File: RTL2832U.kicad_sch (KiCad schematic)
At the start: 35 parts, among them U3 RTL2832U, U4 M24C02-WMN

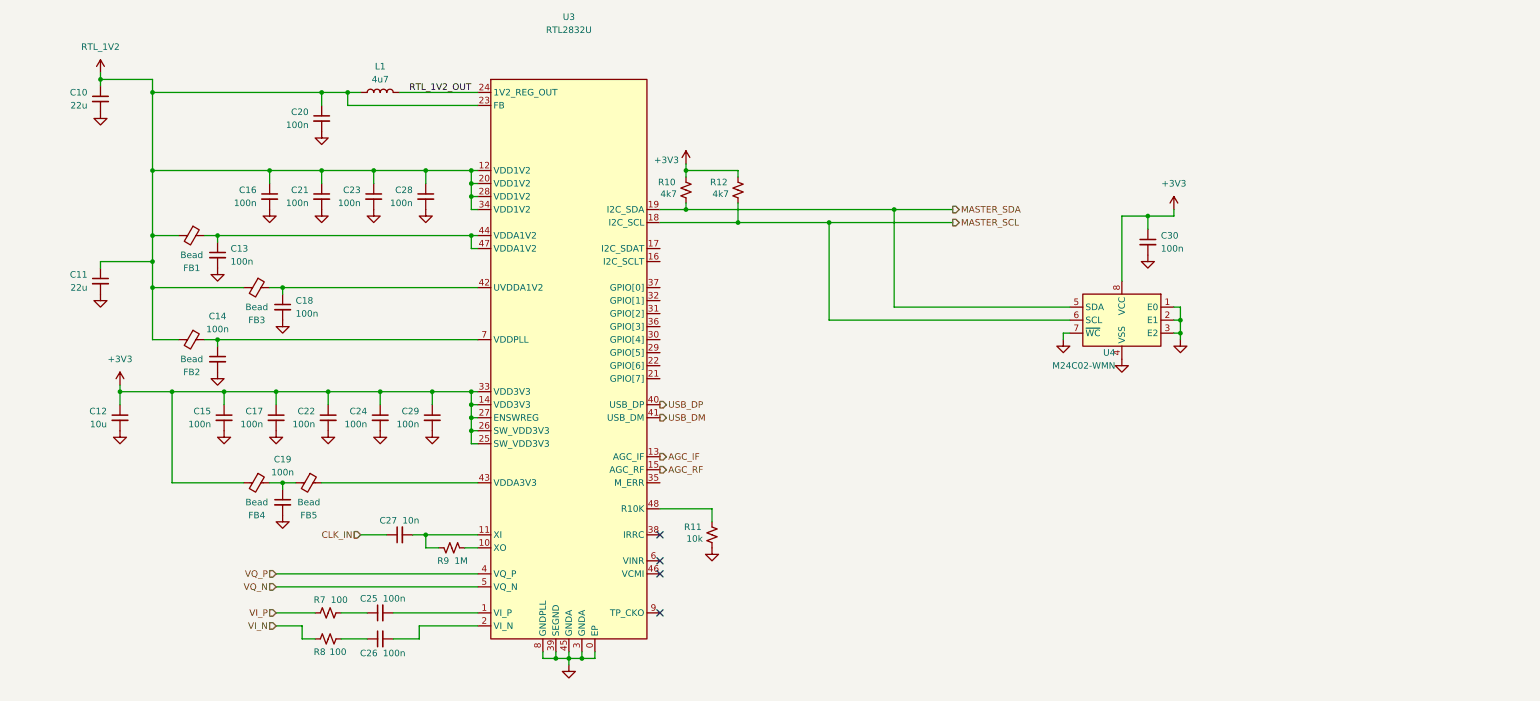
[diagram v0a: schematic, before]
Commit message: Schematic progress
I keep forgetting that I'm just making a panadapter here and not a full blown SDR...oops
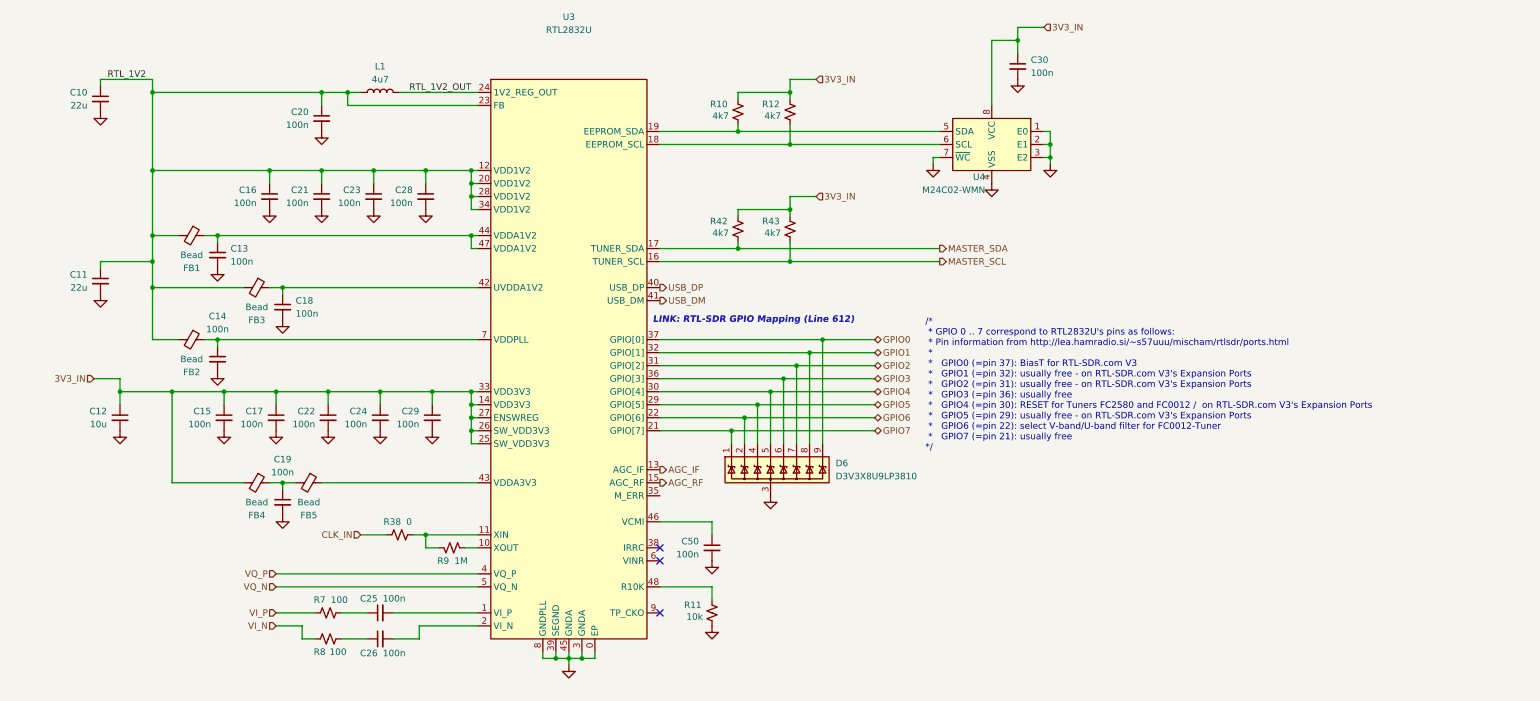
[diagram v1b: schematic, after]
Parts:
- removed C27: 10n, libraries:Worthington_C_0402, symbol Device:C_Small
- added C50: 100n, libraries:Worthington_C_0402, symbol Device:C_Small
- added D6: D3V3X8U9LP3810, Package_DFN_QFN:Diodes_UDFN3810-9_TYPE_B, symbol Power_Protection:D3V3X8U9LP3810
- added R38: 0, libraries:Worthington_R_0402, symbol Device:R_Small_US
- added R42, R43: 4k7, libraries:Worthington_R_0402, symbol Device:R_Small_US
- R10, R11, R12, R7, R8, R9: footprint (none) -> libraries:Worthington_R_0402
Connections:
- net CLK_IN: now also R38.1
- net GND: now also C50.2, D6.3 (GND)
- net MASTER_SCL: now also U3.16 (TUNER_SCL), R43.1; no longer R12.1, U3.18 (I2C_SCL), U4.6 (SCL)
- net MASTER_SDA: now also U3.17 (TUNER_SDA), R42.1; no longer R10.1, U3.19 (I2C_SDA), U4.5 (SDA)
- net at R9.1, U3.11 (XIN): now also R38.2
- net GPIO7: now reaches U3.21 (GPIO[7])
- net GPIO7: now also D6.1 (Line-1)
- net GPIO6: now reaches U3.22 (GPIO[6])
- net GPIO6: now also D6.2 (Line-3)
- net GPIO5: now reaches U3.29 (GPIO[5])
- net GPIO5: now also D6.4 (Line-6)
- net GPIO4: now reaches U3.30 (GPIO[4])
- net GPIO4: now also D6.5 (Line-8)
- net GPIO2: now reaches U3.31 (GPIO[2])
- net GPIO2: now also D6.7 (Line-5)
- net GPIO1: now reaches U3.32 (GPIO[1])
- net GPIO1: now also D6.8 (Line-4)
- net GPIO3: now reaches U3.36 (GPIO[3])
- net GPIO3: now also D6.6 (Line-7)
- net GPIO0: now reaches U3.37 (GPIO[0])
- net GPIO0: now also D6.9 (Line-2)
- net at U3.46 (VCMI): now also C50.1
- net +3V3 renamed 3V3_IN
- net 3V3_IN: now also R42.2, R43.2
- new net: R12.1, U3.18 (EEPROM_SCL), U4.6 (SCL)
- new net: R10.1, U3.19 (EEPROM_SDA), U4.5 (SDA)
- no-connect marks 4 -> 3
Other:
- note added: "/* * GPIO 0 .. 7 correspond to RTL2832U's pins as follows: * Pin information from http://lea.hamradio.si/~s57uuu/mischam/rtlsdr/ports.html * * GPIO0 (=pin 37): BiasT for RTL-SDR.com V3 * GPIO1 (=pin 32): usually free - on RTL-SDR.com V3's Expansion Ports * GPIO2 (=pin 31): usually free - on RTL-SDR.com V3's Expansion Ports * GPIO3 (=pin 36): usually free * GPIO4 (=pin 30): RESET for Tuners FC2580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"
- note added: "LINK: RTL-SDR GPIO Mapping (Line 612)"
- moved on the sheet: C30, R10, R11, R12, U4

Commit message: Schematic progress
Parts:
- added C90, C91: 100n, libraries:Worthington_C_0402, symbol Device:C_Small
- added R37, R68: 100, libraries:Worthington_R_0402, symbol Device:R_Small_US
- added R69, R70: 50, libraries:Worthington_R_0402, symbol Device:R_Small_US
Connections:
- net VI_N: now also R70.1
- net VI_P: now also R70.2
- net VQ_N: now also R68.2, R69.1; no longer U3.5 (VQ_N)
- net VQ_P: now also R37.1, R69.2; no longer U3.4 (VQ_P)
- new net: C90.1, R37.2
- new net: C90.2, U3.4 (VQ_P)
- new net: C91.2, U3.5 (VQ_N)
- new net: C91.1, R68.1
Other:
- note added: "90-Ohm Trace Impedance"
- moved on the sheet: C25, C26, R7, R8, U3

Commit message: Schematic progress
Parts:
- removed C10, C11: 22u, libraries:Worthington_C_0603, symbol Device:C_Small
- removed C12: 10u, libraries:Worthington_C_0603, symbol Device:C_Small
- removed C13, C14, C15, C16, C17, C18, C19, C20, C21, C22, C23, C24, C25, C26, C28, C29, C30, C50: 100n, libraries:Worthington_C_0402, symbol Device:C_Small
- removed R10, R12: 4k7, libraries:Worthington_R_0402, symbol Device:R_Small_US
- removed R38: 0, libraries:Worthington_R_0402, symbol Device:R_Small_US
- added C100, C101, C102, C103, C104, C105, C106, C107, C108, C109, C110, C111, C112, C113, C114, C115, C124, C98, C99: 100n, libraries:Worthington_C_0201, symbol Device:C_Small
- added C125, C126, C53: 10u, libraries:Worthington_C_0402, symbol Device:C_Small
- added R73, R74: 4k7, libraries:Worthington_R_0201, symbol Device:R_Small_US
- added R75, R76: 0, libraries:Worthington_R_0201, symbol Device:R_Small_US
- C90, C91: footprint libraries:Worthington_C_0402 -> libraries:Worthington_C_0201; DigiKey (none) -> 445-15903-1-ND; Manufacturer Part Number (none) -> C0603X6S1C104K030BC; Voltage (none) -> 16V
- FB1, FB2, FB3, FB4, FB5: footprint (none) -> libraries:Worthington_L_0402; now not fitted
- L1: value 4u7 -> 4u7,±20%; footprint Inductor_SMD:L_0805_2012Metric -> Inductor_SMD:L_1008_2520Metric; Current (none) -> 1.5A; DC Resistance (none) -> 180 mOhm; DigiKey (none) -> 3526-WIP252012S-4R7MLDGCT-ND; Manufacturer Part Number (none) -> WIP252012S-4R7MLDG
- R11, R37, R42, R43, R68, R7, R8: footprint libraries:Worthington_R_0402 -> libraries:Worthington_R_0201
- R9: footprint libraries:Worthington_R_0402 -> libraries:Worthington_R_0201; now not fitted
- renumbered D6 to DN1
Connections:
- net 3V3_IN: now also C100.1, C101.1, C102.1, C115.1, C53.1, C98.1, C99.1, R73.2, R74.2, R75.2; no longer U3.27 (ENSWREG)
- net CLK_IN: now also C124.1
- net GND: now also R11.2, C100.2, C101.2, C102.2, C103.2, C104.2, C105.2, C106.2, C107.2, C108.2, C109.2, C110.2, C111.2, C114.2, C115.2, C125.2, C126.2, C53.2, C98.2, C99.2, R76.2; no longer R11.1
- net RTL_1V2: now also C105.1, C106.1, C107.1, C108.1, C109.1, C125.1, C126.1
- net at R7.2: now also C112.1
- net at U3.18 (EEPROM_SCL), U4.6 (SCL): now also R74.1
- net at U3.1 (VI_P): now also C112.2
- net at R9.1, U3.11 (XIN): now also C124.2
- net at U3.48 (R10K): now also R11.1; no longer R11.2
- net at FB4.1, FB5.2: now also C111.1
- net at U3.19 (EEPROM_SDA), U4.5 (SDA): now also R73.1
- net at U3.2 (VI_N): now also C113.2
- net at FB3.1, U3.42 (UVDDA1V2): now also C103.1
- net at FB1.1, U3.44 (VDDA1V2), U3.47 (VDDA1V2): now also C104.1
- net at U3.46 (VCMI): now also C114.1
- net at FB2.1, U3.7 (VDDPLL): now also C110.1
- net at R8.1: now also C113.1
- new net: R75.1, R76.1, U3.27 (ENSWREG)
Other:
- moved on the sheet: R11

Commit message: Schematic and PCB progress
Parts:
- R6: renamed from R69; footprint libraries:Worthington_R_0402 -> libraries:Worthington_R_0201
- R7: renamed from R70; footprint libraries:Worthington_R_0402 -> libraries:Worthington_R_0201
- renumbered C91 to C10, C112 to C11, C113 to C12, C108 to C13, C101 to C14, C111 to C15, C103 to C16, C109 to C17, C107 to C18, C100 to C19, C106 to C20, C110 to C21, C99 to C22, C124 to C23, C105 to C24, C98 to C25, C114 to C26, C115 to C27, C126 to C4, C125 to C5, C53 to C6, C104 to C7, C102 to C8, C90 to C9, FB4 to FB2, FB2 to FB4, R7 to R10, R8 to R11, R76 to R12, R9 to R13, R75 to R14, R11 to R15, R73 to R16, R42 to R17, R74 to R18, R43 to R19, R37 to R8, R68 to R9, U3 to U5, U4 to U6
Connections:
- net GND: now also U5.49 (EP); no longer U5.0 (EP)

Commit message: PCB Layout Progress
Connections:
- net VI_N: now also R9.2; no longer R11.2, R7.1
- net VI_P: now also R8.1; no longer R10.1, R7.2
- net VQ_N: now also R11.2; no longer R6.1, R9.2
- net VQ_P: now also R10.1; no longer R6.2, R8.1
- net at C11.2: now also R7.2, U5.4 (VQ_P); no longer U5.1 (VI_P)
- net at C10.2: now also R6.1, U5.2 (VI_N); no longer U5.5 (VQ_N)
- net at C12.2: now also R7.1, U5.5 (VQ_N); no longer U5.2 (VI_N)
- net at C9.2: now also R6.2, U5.1 (VI_P); no longer U5.4 (VQ_P)
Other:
- moved on the sheet: R6, R7
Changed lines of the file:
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@@
 	)
 	(junction
+		(at 143.51 195.58)
+		(diameter 0)
+		(color 0 0 0 0)
+	)
+	(junction
 		(at 167.64 152.4)
 		(diameter 0)
@@
 	)
 	(junction
-		(at 97.79 182.88)
-		(diameter 0)
-		(color 0 0 0 0)
-	)
-	(junction
 		(at 236.22 139.7)
 		(diameter 0)
@@
 	)
 	(junction
+		(at 143.51 182.88)
+		(diameter 0)
+		(color 0 0 0 0)
+	)
+	(junction
 		(at 184.15 204.47)
 		(diameter 0)
@@
 	)
 	(junction
+		(at 143.51 200.66)
+		(diameter 0)
+		(color 0 0 0 0)
+	)
+	(junction
 		(at 138.43 106.68)
 		(diameter 0)
@@
 	)
 	(junction
-		(at 97.79 187.96)
+		(at 231.14 144.78)
 		(diameter 0)
 		(color 0 0 0 0)
 	)
 	(junction
-		(at 231.14 144.78)
+		(at 143.51 187.96)
 		(diameter 0)
 		(color 0 0 0 0)
@@
 	)
 	(junction
-		(at 97.79 200.66)
-		(diameter 0)
-		(color 0 0 0 0)
-	)
-	(junction
 		(at 105.41 124.46)
 		(diameter 0)
@@
 	)
 	(junction
-		(at 97.79 195.58)
-		(diameter 0)
-		(color 0 0 0 0)
-	)
-	(junction
 		(at 167.64 119.38)
 		(diameter 0)
@@
 	(wire
 		(pts
-			(xy 85.09 187.96) (xy 97.79 187.96)
+			(xy 85.09 187.96) (xy 107.95 187.96)
 		)
 		(stroke
@@
 	(wire
 		(pts
-			(xy 128.27 195.58) (xy 168.91 195.58)
+			(xy 128.27 195.58) (xy 143.51 195.58)
 		)
 		(stroke
@@
 	(wire
 		(pts
+			(xy 143.51 200.66) (xy 157.48 200.66)
+		)
+		(stroke
+			(width 0)
+			(type default)
+		)
+	)
+	(wire
+		(pts
 			(xy 231.14 160.02) (xy 231.14 144.78)
 		)
@@
 	(wire
 		(pts
-			(xy 85.09 200.66) (xy 97.79 200.66)
+			(xy 85.09 200.66) (xy 107.95 200.66)
 		)
 		(stroke
@@
 	(wire
 		(pts
-			(xy 97.79 182.88) (xy 107.95 182.88)
-		)
-		(stroke
-			(width 0)
-			(type default)
-		)
-	)
-	(wire
-		(pts
-			(xy 85.09 195.58) (xy 97.79 195.58)
+			(xy 85.09 195.58) (xy 107.95 195.58)
 		)
 		(stroke
@@
 	(wire
 		(pts
-			(xy 128.27 200.66) (xy 157.48 200.66)
+			(xy 128.27 200.66) (xy 143.51 200.66)
 		)
 		(stroke
@@
 	(wire
 		(pts
+			(xy 143.51 195.58) (xy 168.91 195.58)
+		)
+		(stroke
+			(width 0)
+			(type default)
+		)
+	)
+	(wire
+		(pts
 			(xy 236.22 139.7) (xy 246.38 139.7)
 		)
@@
 	(wire
 		(pts
-			(xy 97.79 195.58) (xy 107.95 195.58)
-		)
-		(stroke
-			(width 0)
-			(type default)
-		)
-	)
-	(wire
-		(pts
 			(xy 229.87 88.9) (xy 229.87 91.44)
 		)
@@
 	(wire
 		(pts
-			(xy 85.09 182.88) (xy 97.79 182.88)
+			(xy 85.09 182.88) (xy 107.95 182.88)
+		)
+		(stroke
+			(width 0)
+			(type default)
+		)
+	)
+	(wire
+		(pts
+			(xy 143.51 182.88) (xy 154.94 182.88)
 		)
 		(stroke
@@
 	(wire
 		(pts
-			(xy 97.79 200.66) (xy 107.95 200.66)
-		)
-		(stroke
-			(width 0)
-			(type default)
-		)
-	)
-	(wire
-		(pts
 			(xy 223.52 152.4) (xy 246.38 152.4)
 		)
@@
 	(wire
 		(pts
-			(xy 97.79 187.96) (xy 107.95 187.96)
+			(xy 143.51 187.96) (xy 168.91 187.96)
 		)
 		(stroke
@@
 	(wire
 		(pts
-			(xy 128.27 187.96) (xy 168.91 187.96)
+			(xy 128.27 187.96) (xy 143.51 187.96)
 		)
 		(stroke
@@
 	(wire
 		(pts
-			(xy 128.27 182.88) (xy 154.94 182.88)
+			(xy 128.27 182.88) (xy 143.51 182.88)
 		)
 		(stroke
@@
 	(hierarchical_label "VI_N"
 		(shape input)
-		(at 85.09 200.66 180)
+		(at 85.09 187.96 180)
 		(effects
 			(font
@@
 	(hierarchical_label "VQ_P"
 		(shape input)
-		(at 85.09 182.88 180)
+		(at 85.09 195.58 180)
 		(effects
 			(font
@@
 	(hierarchical_label "VQ_N"
 		(shape input)
-		(at 85.09 187.96 180)
+		(at 85.09 200.66 180)
 		(effects
 			(font
@@
 	(hierarchical_label "VI_P"
 		(shape input)
-		(at 85.09 195.58 180)
+		(at 85.09 182.88 180)
 		(effects
 			(font
@@
 	(symbol
 		(lib_id "Device:R_Small_US")
-		(at 97.79 185.42 180)
+		(at 143.51 185.42 180)
 		(unit 1)
 		(body_style 1)
@@
 		(dnp yes)
 		(property "Reference" "R6"
-			(at 95.758 183.896 0)
+			(at 141.478 183.896 0)
 			(show_name no)
 			(do_not_autoplace no)
@@
 		)
 		(property "Value" "50"
-			(at 96.012 186.182 0)
+			(at 141.732 186.182 0)
 			(show_name no)
 			(do_not_autoplace no)
@@
 		)
 		(property "Footprint" "libraries:Worthington_R_0201"
-			(at 97.79 185.42 0)
+			(at 143.51 185.42 0)
 			(hide yes)
 			(show_name no)
@@
 		)
 		(property "Datasheet" ""
-			(at 97.79 185.42 0)
+			(at 143.51 185.42 0)
 			(hide yes)
 			(show_name no)
@@
 		)
 		(property "Description" "Resistor, small US symbol"
-			(at 97.79 185.42 0)
+			(at 143.51 185.42 0)
 			(hide yes)
 			(show_name no)
@@
 	(symbol
 		(lib_id "Device:R_Small_US")
-		(at 97.79 198.12 180)
+		(at 143.51 198.12 180)
 		(unit 1)
 		(body_style 1)
@@
 		(dnp yes)
 		(property "Reference" "R7"
-			(at 95.758 196.596 0)
+			(at 141.478 196.596 0)
 			(show_name no)
 			(do_not_autoplace no)
@@
 		)
 		(property "Value" "50"
-			(at 96.012 198.882 0)
+			(at 141.732 198.882 0)
 			(show_name no)
 			(do_not_autoplace no)
@@
 		)
 		(property "Footprint" "libraries:Worthington_R_0201"
-			(at 97.79 198.12 0)
+			(at 143.51 198.12 0)
 			(hide yes)
 			(show_name no)
@@
 		)
 		(property "Datasheet" ""
-			(at 97.79 198.12 0)
+			(at 143.51 198.12 0)
 			(hide yes)
 			(show_name no)
@@
 		)
 		(property "Description" "Resistor, small US symbol"
-			(at 97.79 198.12 0)
+			(at 143.51 198.12 0)
 			(hide yes)
 			(show_name no)

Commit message: PCB and schematic progress
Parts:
- removed DN1: D3V3X8U9LP3810, Package_DFN_QFN:Diodes_UDFN3810-9_TYPE_B, symbol Power_Protection:D3V3X8U9LP3810
- removed FB1, FB2, FB3, FB4, FB5: Bead, libraries:Worthington_L_0402, symbol Device:FerriteBead_Small
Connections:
- net 3V3_IN: now also C15.1, U5.43 (VDDA3V3); no longer C8.1
- net RTL_1V2: now also C16.1, C21.1, C7.1, C8.1, U5.42 (UVDDA1V2), U5.44 (VDDA1V2), U5.47 (VDDA1V2), U5.7 (VDDPLL)
- no-connect marks 3 -> 4

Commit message: PCB and schematic progress
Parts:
- removed C27: 100n, libraries:Worthington_C_0201, symbol Device:C_Small
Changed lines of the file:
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@@
 	)
 	(junction
-		(at 274.32 81.28)
-		(diameter 0)
-		(color 0 0 0 0)
-	)
-	(junction
 		(at 109.22 149.86)
 		(diameter 0)
@@
 	(wire
 		(pts
-			(xy 274.32 81.28) (xy 274.32 83.82)
-		)
-		(stroke
-			(width 0)
-			(type default)
-		)
-	)
-	(wire
-		(pts
 			(xy 128.27 119.38) (xy 167.64 119.38)
 		)
@@
 	)
 	(symbol
-		(lib_id "power:GND")
-		(at 274.32 88.9 0)
-		(unit 1)
-		(body_style 1)
-		(exclude_from_sim no)
-		(in_bom yes)
-		(on_board yes)
-		(in_pos_files yes)
-		(dnp no)
-		(fields_autoplaced yes)
-		(property "Reference" "#PWR055"
-			(at 274.32 95.25 0)
-			(hide yes)
-			(show_name no)
-			(do_not_autoplace no)
-			(effects
-				(font
-					(size 1.27 1.27)
-				)
-			)
-		)
-		(property "Value" "GND"
-			(at 274.32 93.98 0)
-			(hide yes)
-			(show_name no)
-			(do_not_autoplace no)
-			(effects
-				(font
-					(size 1.27 1.27)
-				)
-			)
-		)
-		(property "Footprint" ""
-			(at 274.32 88.9 0)
-			(hide yes)
-			(show_name no)
-			(do_not_autoplace no)
-			(effects
-				(font
-					(size 1.27 1.27)
-				)
-			)
-		)
-		(property "Datasheet" ""
-			(at 274.32 88.9 0)
-			(hide yes)
-			(show_name no)
-			(do_not_autoplace no)
-			(effects
-				(font
-					(size 1.27 1.27)
-				)
-			)
-		)
-		(property "Description" "Power symbol creates a global label with name \"GND\" , ground"
-			(at 274.32 88.9 0)
-			(hide yes)
-			(show_name no)
-			(do_not_autoplace no)
-			(effects
-				(font
-					(size 1.27 1.27)
-				)
-			)
-		)
-		(pin "1"
-		)
-		(instances
-			(project "PiZero_RTL_Panadapter"
-				(path "/9dbbaad8-804a-4efe-a989-bc17c5acbd91/78a19d34-3089-4e0b-b1d1-ac7541a92b32"
-					(reference "#PWR055")
-					(unit 1)
-				)
-			)
-		)
-	)
-	(symbol
 		(lib_id "Device:C_Small")
 		(at 129.54 154.94 0)
@@
 					(unit 1)
 				)
-			)
-		)
-	)
-	(symbol
-		(lib_id "Device:C_Small")
-		(at 274.32 86.36 0)
-		(unit 1)
-		(body_style 1)
-		(exclude_from_sim no)
-		(in_bom yes)
-		(on_board yes)
-		(in_pos_files yes)
-		(dnp no)
-		(property "Reference" "C27"
-			(at 276.86 85.0962 0)
-			(show_name no)
-			(do_not_autoplace no)
-			(effects
-				(font
-					(size 1.27 1.27)
-				)
-				(justify left)
-			)
-		)
-		(property "Value" "100n"
-			(at 276.86 87.6362 0)
-			(show_name no)
-			(do_not_autoplace no)
-			(effects
-				(font
-					(size 1.27 1.27)
-				)
-				(justify left)
-			)
-		)
-		(property "Footprint" "libraries:Worthington_C_0201"
-			(at 274.32 86.36 0)
-			(hide yes)
-			(show_name no)
-			(do_not_autoplace no)
-			(effects
-				(font
-					(size 1.27 1.27)
-				)
-			)
-		)
-		(property "Datasheet" "https://product.tdk.com/system/files/dam/doc/product/capacitor/ceramic/mlcc/catalog/mlcc_commercial_general_en.pdf"
-			(at 274.32 86.36 0)
-			(hide yes)
-			(show_name no)
-			(do_not_autoplace no)
-			(effects
-				(font
-					(size 1.27 1.27)
-				)
-			)
-		)
-		(property "Description" "Unpolarized capacitor, small symbol"
-			(at 274.32 86.36 0)
-			(hide yes)
-			(show_name no)
-			(do_not_autoplace no)
-			(effects
-				(font
-					(size 1.27 1.27)
-				)
-			)
-		)
-		(property "Manufacturer Part Number" "C0603X6S1C104K030BC"
-			(at 274.32 86.36 0)
-			(hide yes)
-			(show_name no)
-			(do_not_autoplace no)
-			(effects
-				(font
-					(size 1.27 1.27)
-				)
-			)
-		)
-		(property "DigiKey" "445-15903-1-ND"
-			(at 274.32 86.36 0)
-			(hide yes)
-			(show_name no)
-			(do_not_autoplace no)
-			(effects
-				(font
-					(size 1.27 1.27)
-				)
-			)
-		)
-		(property "Voltage" "16V"
-			(at 278.892 90.17 0)
-			(show_name no)
-			(do_not_autoplace no)
-			(effects
-				(font
-					(size 1.27 1.27)
-				)
-			)
-		)
-		(pin "1"
-		)
-		(pin "2"
-		)
-		(instances
-			(project "PiZero_RTL_Panadapter"
-				(path "/9dbbaad8-804a-4efe-a989-bc17c5acbd91/78a19d34-3089-4e0b-b1d1-ac7541a92b32"
-					(reference "C27")
-					(unit 1)
-				)

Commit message: Small PCB layout tweaks
Beautification, if you will...
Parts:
- R12, R14: value 0 -> 0R
- R6, R7: value 50 -> 49.9
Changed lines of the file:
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@@
 			)
 		)
-		(property "Value" "0"
+		(property "Value" "0R"
 			(at 162.052 164.592 90)
 			(show_name no)
@@
 			)
 		)
-		(property "Value" "50"
+		(property "Value" "49.9"
 			(at 141.732 186.182 0)
 			(show_name no)
@@
 			)
 		)
-		(property "Value" "0"
+		(property "Value" "0R"
 			(at 165.862 160.782 0)
 			(show_name no)
@@
 			)
 		)
-		(property "Value" "50"
+		(property "Value" "49.9"
 			(at 141.732 198.882 0)
 			(show_name no)
